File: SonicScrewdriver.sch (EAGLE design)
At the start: 63 parts, among them IC1 LD1117AS33TR, IC2 MCP6004, IC3 LD1117AS33TR, IC5 LM4040B10, Q2 MMBT3904, U1 MKL02Z32VFK4, X1 CRYSTAL-0500290P1

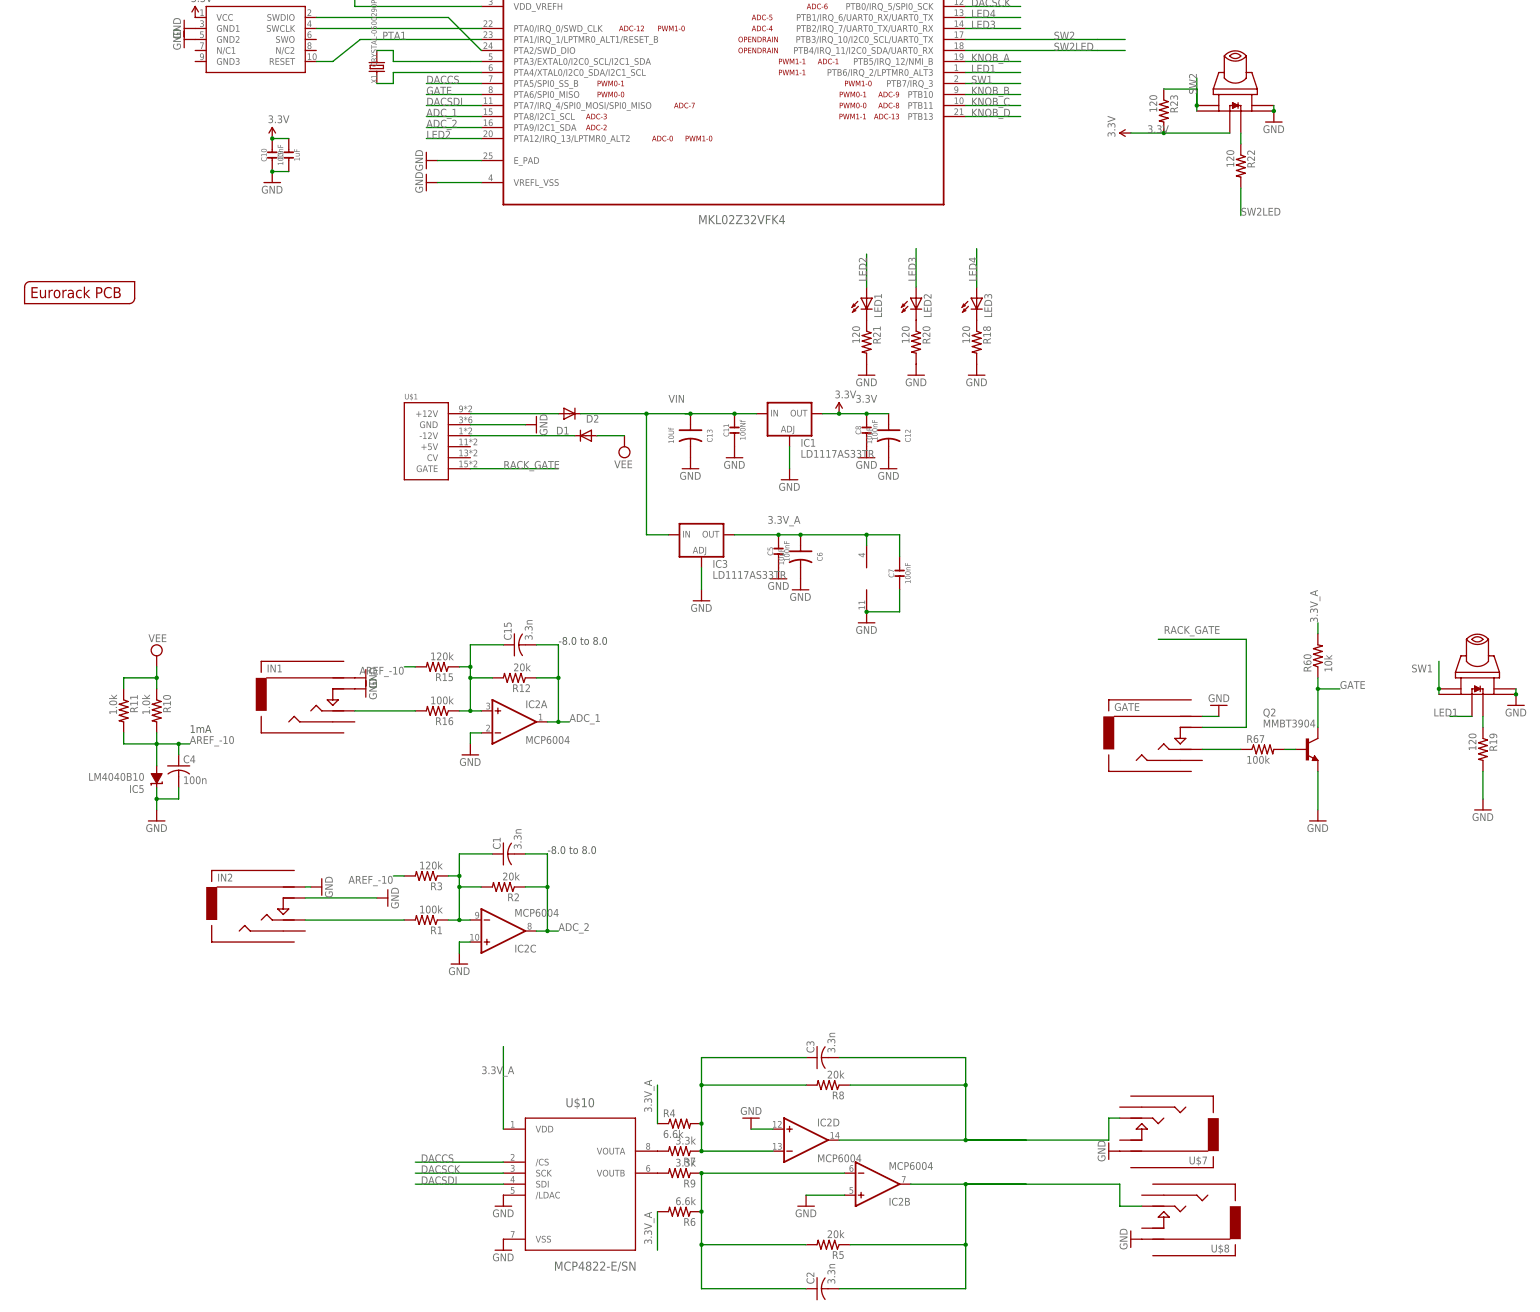
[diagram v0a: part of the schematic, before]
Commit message: Renamed LogicThingie to SonicScrewdriver - cosmetic changes, panel exports, cam folders
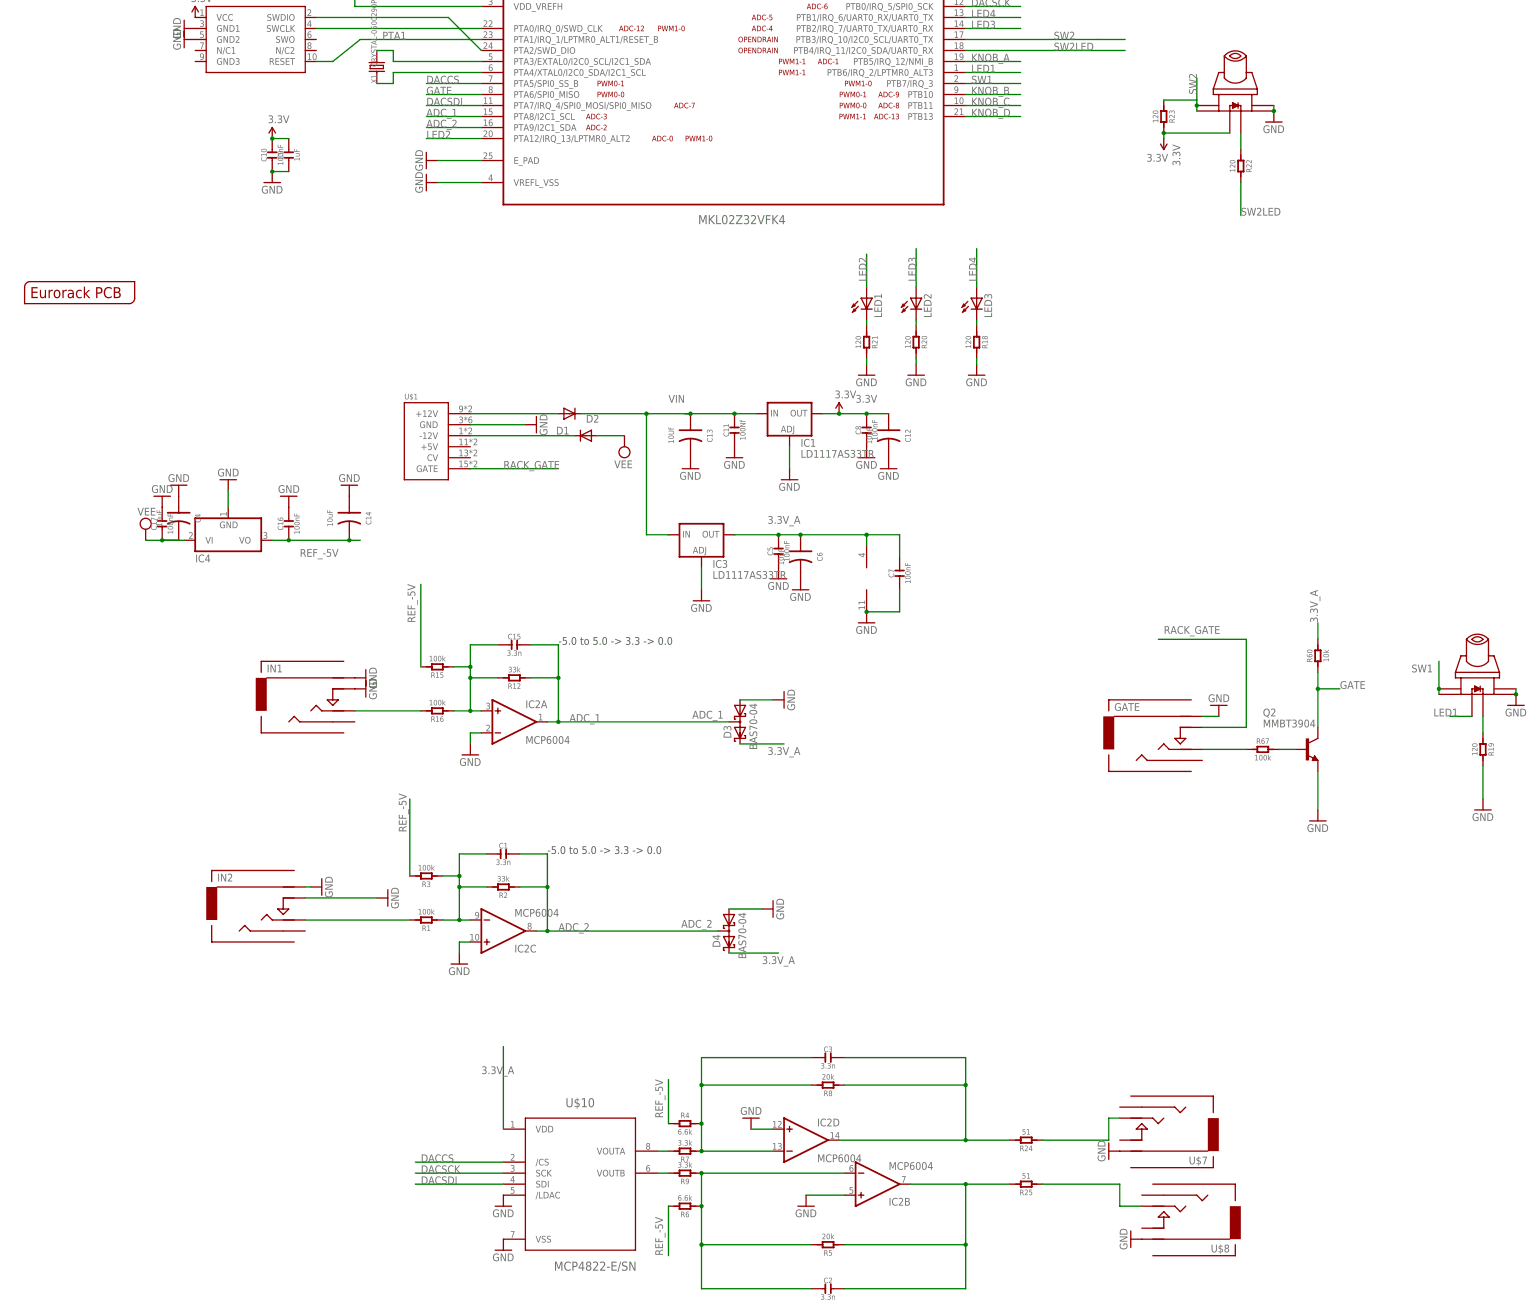
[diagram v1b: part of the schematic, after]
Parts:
- removed IC5: LM4040B10, texas:LM4041B12DBZ
- removed R10, R11: 1.0k, rcl:R-US_R0603
- added C14: 10uF, OPL:C-POLAR-A
- added C16, C17: 100nF, OPL:C-0603
- added D3, D4: BAS70-04, diode:BAS70-04
- added IC4: (no value), linear:7905T
- added R24, R25: 51, OPL:R-0603
- C1, C15, C2, C3: device rcl:C-USC0603 -> OPL:C-0603
- C4: value 100n -> 10uF; device rcl:C-USC0603 -> OPL:C-POLAR-A
- R1, R16, R18, R19, R20, R21, R22, R23, R4, R5, R6, R60, R67, R7, R8, R9: device rcl:R-US_R0603 -> OPL:R-0603
- R12, R2: value 20k -> 33k; device rcl:R-US_R0603 -> OPL:R-0603
- R15, R3: value 120k -> 100k; device rcl:R-US_R0603 -> OPL:R-0603
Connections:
- removed net AREF_-10: C4.1, IC5.A, R10.2, R11.2, R15.2, R3.2
- new net N$20: R25.1, U$8.TIP
- new net N$21: R24.1, U$7.TIP
- new net REF_-5V: C14.2, C16.1, IC4.VO, R15.2, R3.2, R4.1, R6.2
- net 3.3V_A: now also D3.C2, D4.C2; no longer R4.1, R6.2
- net ADC_1: now also D3.C1A2
- net ADC_2: now also D4.C1A2
- net GND: now also C14.1, C16.2, C17.2, C4.1, D3.A1, D4.A1, IC4.GND; no longer C4.2, IC5.C
- net N$18: now also R24.2; no longer U$7.TIP
- net N$24: now also R25.2; no longer U$8.TIP
- net VEE: now also C17.1, C4.2, IC4.VI; no longer R10.1, R11.1
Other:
- note added: "-5.0 to 5.0 -> 3.3 -> 0.0"
- note removed: "-8.0 to 8.0"
- note removed: "1mA"

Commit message: pre order fixes
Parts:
- IC4: value (none) -> 7905
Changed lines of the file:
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@@
 <part name="R24" library="OPL" deviceset="R*" device="-0603" value="51"/>
 <part name="R25" library="OPL" deviceset="R*" device="-0603" value="51"/>
-<part name="IC4" library="linear" deviceset="79*" device="T" technology="05"/>
+<part name="IC4" library="linear" deviceset="79*" device="T" technology="05" value="7905"/>
 <part name="GND38" library="SparkFun-Aesthetics" deviceset="GND" device=""/>
 <part name="SUPPLY1" library="supply2" deviceset="VEE" device=""/>
@@
 <wire x1="314.96" y1="72.39" x2="322.58" y2="72.39" width="0.1524" layer="91"/>
 <wire x1="322.58" y1="72.39" x2="322.58" y2="71.12" width="0.1524" layer="91"/>
-</segment>
-</net>
+<junction x="322.58" y="72.39"/>
+</segment>
+</net>
